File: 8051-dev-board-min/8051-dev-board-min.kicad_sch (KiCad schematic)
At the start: 8 parts, among them SW1 RESET, U1 AT89S4051-24P, Y1 11.0592MHz

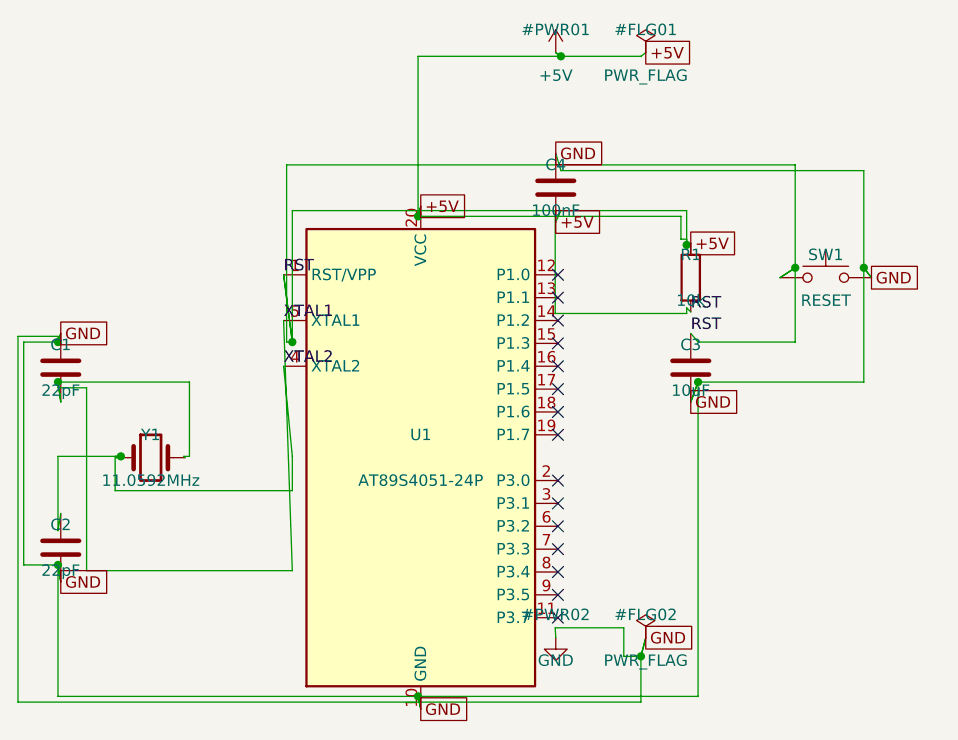
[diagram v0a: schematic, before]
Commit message: Schematic autorouting: pin_xy alignment, pipeline, and KiCad apply fixes
- Emit pin_xy from KiCad converter; load in schematic_data and place pins in cad_viewer so routed wires match library pin positions.
- Add end-to-end pipeline.py (strip, convert, route, apply with backups).
- apply_routes_to_kicad_sch: orthogonalize polylines for KiCad-native wires.
- cad_viewer: pin tunnels, waypoint snap export, optional native A* batch path.
- kicad_sch_to_schematic_json: connectivity and pin geometry for wire-free nets.
- docs/pcb-schematic-basics.md: schematic/PCB vocabulary reference.
- Refresh 8051-dev-board-min example schematic, JSON, and routes after pipeline run.

Co-authored-by: Cursor <cursoragent@cursor.com>
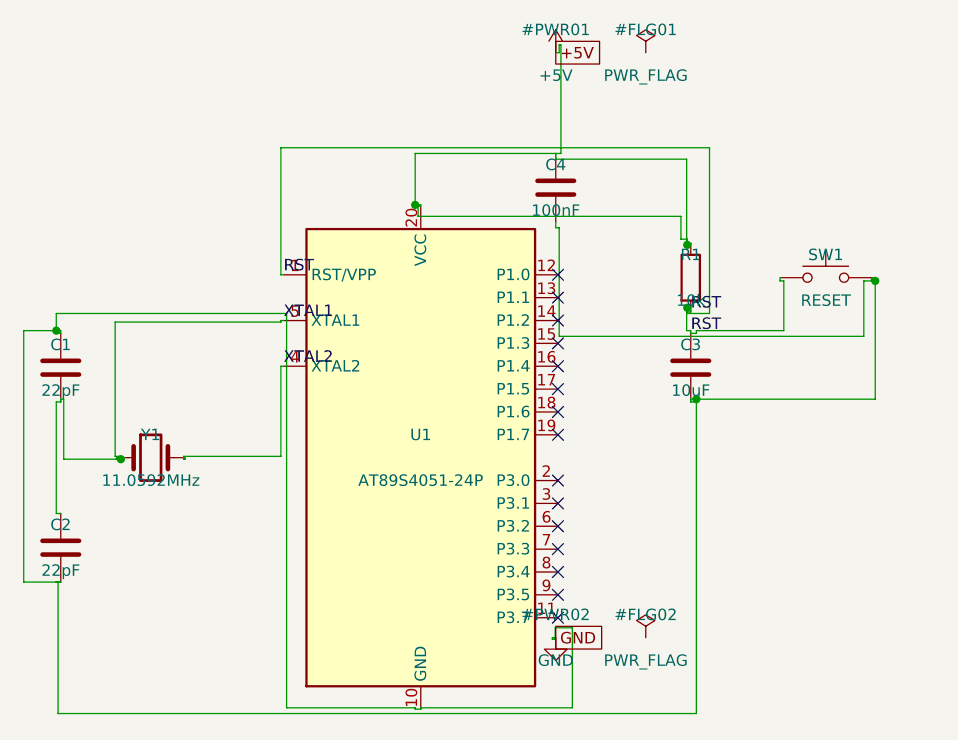
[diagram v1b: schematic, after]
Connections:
- net +5V: now also C4.1; no longer C4.2
- net GND: now also C4.2; no longer C4.1
- net XTAL1: now also C2.1, Y1.1; no longer Y1.2
- net XTAL2: now also Y1.2; no longer C2.1, Y1.1
